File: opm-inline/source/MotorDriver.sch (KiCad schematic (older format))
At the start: 38 parts, among them IC1 TMC6200-TA, Q1 HYG025N06LS1C2, Q2 HYG025N06LS1C2, Q3 HYG025N06LS1C2, Q4 HYG025N06LS1C2, Q5 HYG025N06LS1C2, Q6 HYG025N06LS1C2

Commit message: update connections
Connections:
- net FAULT: now reaches IC1.26 (FAULT)
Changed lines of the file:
@@
 $Descr A4 11693 8268
 encoding utf-8
-Sheet 3 3
+Sheet 2 3
 Title "TMC6100-EVAL"
 Date "2019-10-28"
@@
 Text HLabel 3650 3400 0    28   Input ~ 0
 SPE
-Text HLabel 4750 3950 2    28   Input ~ 0
+Text HLabel 4750 3950 2    28   Output ~ 0
 ADC_I_u
-Text HLabel 4750 4000 2    28   Input ~ 0
+Text HLabel 4750 4000 2    28   Output ~ 0
 ADC_I_v
-Text HLabel 4750 4050 2    28   Input ~ 0
+Text HLabel 4750 4050 2    28   Output ~ 0
 ADC_I_w
 $Comp
@@
 	1    0    0    -1
 $EndComp
-Text HLabel 8750 2200 2    31   Input ~ 0
+Text HLabel 8750 2200 2    31   Output ~ 0
 U
 Wire Wire Line
 	8500 2200 8750 2200
-Text HLabel 10450 3500 2    31   Input ~ 0
+Text HLabel 10450 3500 2    31   Output ~ 0
 V
 Wire Wire Line
 	10150 3500 10450 3500
-Text HLabel 8800 5000 2    31   Input ~ 0
+Text HLabel 8800 5000 2    31   Output ~ 0
 W
 Wire Wire Line
@@
 	3650 3650 3450 3650
 $Comp
-L power:GND #PWR?
+L power:GND #PWR0109
 U 1 1 61F1E038
 P 3150 3550
-F 0 "#PWR?" H 3150 3300 39  0001 C CNN
+F 0 "#PWR0109" H 3150 3300 39  0001 C CNN
 F 1 "GND" H 3150 3400 39  0000 C CNN
 F 2 "" H 3150 3550 39  0001 C CNN
@@
 $EndComp
 $Comp
-L power:GND #PWR?
+L power:GND #PWR0113
 U 1 1 61F1F1E2
 P 3400 3500
-F 0 "#PWR?" H 3400 3250 39  0001 C CNN
+F 0 "#PWR0113" H 3400 3250 39  0001 C CNN
 F 1 "GND" H 3400 3350 39  0000 C CNN
 F 2 "" H 3400 3500 39  0001 C CNN
@@
 Wire Wire Line
 	3650 3500 3400 3500
+Text HLabel 4850 4400 3    28   Output ~ 0
+FAULT
+Text HLabel 4800 4400 3    28   Output ~ 0
+FAULT_LED
+Wire Wire Line
+	4800 4400 4800 4300
+Wire Wire Line
+	4800 4300 4750 4300
+Wire Wire Line
+	4800 4300 4850 4300
+Wire Wire Line
+	4850 4300 4850 4400
+Connection ~ 4800 4300
 $EndSCHEMATC

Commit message: rearrange
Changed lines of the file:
@@
 Text HLabel 4750 3950 2    28   Output ~ 0
 ADC_I_u
-Text HLabel 4750 4000 2    28   Output ~ 0
-ADC_I_v
 Text HLabel 4750 4050 2    28   Output ~ 0
 ADC_I_w
@@
 	4850 4300 4850 4400
 Connection ~ 4800 4300
+Text HLabel 4750 4000 2    31   Output ~ 0
+ADC_I_v
 $EndSCHEMATC

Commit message: use pins
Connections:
- net +VCC_IO: no longer IC1.16 (SDO_SINGLE)
- net GND: now also IC1.16 (SDO_SINGLE)
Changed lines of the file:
@@
 Wire Wire Line
 	8500 5000 8800 5000
-Text HLabel 3450 3650 0    31   Input ~ 0
-+VCC_IO
 Text HLabel 3450 3600 0    31   Input ~ 0
 +VCC_IO
@@
 Text HLabel 4850 4400 3    28   Output ~ 0
 FAULT
-Text HLabel 4800 4400 3    28   Output ~ 0
-FAULT_LED
-Wire Wire Line
-	4800 4400 4800 4300
-Wire Wire Line
-	4800 4300 4750 4300
-Wire Wire Line
-	4800 4300 4850 4300
 Wire Wire Line
 	4850 4300 4850 4400
-Connection ~ 4800 4300
 Text HLabel 4750 4000 2    31   Output ~ 0
 ADC_I_v
+$Comp
+L power:GND #PWR0106
+U 1 1 61E2421A
+P 3450 3650
+F 0 "#PWR0106" H 3450 3400 39  0001 C CNN
+F 1 "GND" H 3450 3500 39  0000 C CNN
+F 2 "" H 3450 3650 39  0001 C CNN
+F 3 "" H 3450 3650 39  0001 C CNN
+	1    3450 3650
+	1    0    0    -1
+$EndComp
+Wire Wire Line
+	4750 4300 4850 4300
 $EndSCHEMATC

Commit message: rearrange
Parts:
- added C21, C22, C23, C24, C25, C26: 1uF/100V, Capacitor_SMD:C_0805_2012Metric, symbol Device:C
- C7, C8, C9: value 4.7uF/100V -> 1uF/100V; footprint Capacitor_SMD:C_1210_3225Metric -> Capacitor_SMD:C_0805_2012Metric
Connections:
- net +VM: now also C21.1, C22.1, C23.1, C24.1, C25.1, C26.1
- net GND: now also C21.2, C22.2, C23.2, C24.2, C25.2, C26.2
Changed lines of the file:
@@
-	1    0    0    -1
-$EndComp
-$Comp
-L Device:C C8
-U 1 1 61C62AF0
-P 7700 4400
-F 0 "C8" H 7815 4435 35  0000 L CNN
-F 1 "4.7uF/100V" H 7815 4366 35  0000 L CNN
-F 2 "Capacitor_SMD:C_1210_3225Metric" H 7738 4250 50  0001 C CNN
-F 3 "https://datasheet.lcsc.com/lcsc/1912111437_Taiyo-Yuden-HMJ325AB7225KMHP_C412614.pdf" H 7700 4400 50  0001 C CNN
-F 4 "C697607" H 7700 4400 50  0001 C CNN "LCSC"
-F 5 "HMK325C7475KN-TE" H 7700 4400 50  0001 C CNN "manf_num  "
-	1    7700 4400
 	1    0    0    -1
 $EndComp
@@
 	0    1    1    0
 $EndComp
-$Comp
-L power:GND #PWR07
-U 1 1 61D8AF46
-P 8800 4200
-F 0 "#PWR07" H 8800 3950 50  0001 C CNN
-F 1 "GND" H 8805 4027 50  0000 C CNN
-F 2 "" H 8800 4200 50  0001 C CNN
-F 3 "" H 8800 4200 50  0001 C CNN
-	1    8800 4200
-	1    0    0    -1
-$EndComp
 Wire Wire Line
 	10150 3650 9900 3650
@@
 	10150 3500 10150 3650
 Connection ~ 10150 3500
-Wire Wire Line
-	8800 4100 8800 4200
 $Comp
 L power:GND #PWR08
@@
 F 3 "" H 9350 3000 50  0001 C CNN
 	1    9350 3000
-	1    0    0    -1
-$EndComp
-$Comp
-L Device:C C9
-U 1 1 61D8AF6F
-P 9350 2800
-F 0 "C9" H 9465 2835 35  0000 L CNN
-F 1 "4.7uF/100V" H 9465 2766 35  0000 L CNN
-F 2 "Capacitor_SMD:C_1210_3225Metric" H 9388 2650 50  0001 C CNN
-F 3 "https://datasheet.lcsc.com/lcsc/1912111437_Taiyo-Yuden-HMJ325AB7225KMHP_C412614.pdf" H 9350 2800 50  0001 C CNN
-F 4 "C697607" H 9350 2800 50  0001 C CNN "LCSC"
-F 5 "HMK325C7475KN-TE" H 9350 2800 50  0001 C CNN "manf_num  "
-	1    9350 2800
 	1    0    0    -1
 $EndComp
@@
 	8800 2550 9350 2550
 $Comp
-L Device:C C7
-U 1 1 61D9B6F4
-P 7700 1450
-F 0 "C7" H 7815 1485 35  0000 L CNN
-F 1 "4.7uF/100V" H 7815 1416 35  0000 L CNN
-F 2 "Capacitor_SMD:C_1210_3225Metric" H 7738 1300 50  0001 C CNN
-F 3 "https://datasheet.lcsc.com/lcsc/1912111437_Taiyo-Yuden-HMJ325AB7225KMHP_C412614.pdf" H 7700 1450 50  0001 C CNN
-F 4 "C697607" H 7700 1450 50  0001 C CNN "LCSC"
-F 5 "HMK325C7475KN-TE" H 7700 1450 50  0001 C CNN "manf_num  "
-	1    7700 1450
-	1    0    0    -1
-$EndComp
-$Comp
 L Device:R R1
 U 1 1 61D9B6BE
@@
 ADC_I_v
 $Comp
+L Device:C C9
+U 1 1 61D8AF6F
+P 9350 2800
+F 0 "C9" H 9465 2835 35  0000 L CNN
+F 1 "1uF/100V" H 9465 2766 35  0000 L CNN
+F 2 "Capacitor_SMD:C_0805_2012Metric" H 9388 2650 50  0001 C CNN
+F 3 "https://datasheet.lcsc.com/lcsc/1912111437_Taiyo-Yuden-HMJ325AB7225KMHP_C412614.pdf" H 9350 2800 50  0001 C CNN
+F 4 "C697607" H 9350 2800 50  0001 C CNN "LCSC"
+F 5 "HMK325C7475KN-TE" H 9350 2800 50  0001 C CNN "manf_num  "
+	1    9350 2800
+	1    0    0    -1
+$EndComp
+$Comp
+L Device:C C7
+U 1 1 61D9B6F4
+P 7700 1450
+F 0 "C7" H 7815 1485 35  0000 L CNN
+F 1 "1uF/100V" H 7815 1416 35  0000 L CNN
+F 2 "Capacitor_SMD:C_0805_2012Metric" H 7738 1300 50  0001 C CNN
+F 3 "https://datasheet.lcsc.com/lcsc/1912111437_Taiyo-Yuden-HMJ325AB7225KMHP_C412614.pdf" H 7700 1450 50  0001 C CNN
+F 4 "C697607" H 7700 1450 50  0001 C CNN "LCSC"
+F 5 "HMK325C7475KN-TE" H 7700 1450 50  0001 C CNN "manf_num  "
+	1    7700 1450
+	1    0    0    -1
+$EndComp
+$Comp
+L Device:C C8
+U 1 1 61C62AF0
+P 7700 4400
+F 0 "C8" H 7815 4435 35  0000 L CNN
+F 1 "1uF/100V" H 7815 4366 35  0000 L CNN
+F 2 "Capacitor_SMD:C_0805_2012Metric" H 7738 4250 50  0001 C CNN
+F 3 "https://datasheet.lcsc.com/lcsc/1912111437_Taiyo-Yuden-HMJ325AB7225KMHP_C412614.pdf" H 7700 4400 50  0001 C CNN
+F 4 "C697607" H 7700 4400 50  0001 C CNN "LCSC"
+F 5 "HMK325C7475KN-TE" H 7700 4400 50  0001 C CNN "manf_num  "
+	1    7700 4400
+	1    0    0    -1
+$EndComp
+Wire Wire Line
+	4800 4300 4850 4300
+Wire Wire Line
+	4800 4300 4750 4300
+Connection ~ 4800 4300
+Wire Wire Line
+	4800 4400 4800 4300
+Text HLabel 4800 4400 3    28   Output ~ 0
+FAULT_LED
+$Comp
 L power:GND #PWR0106
 U 1 1 61E2421A
@@
 	1    0    0    -1
 $EndComp
-Wire Wire Line
-	4750 4300 4850 4300
+$Comp
+L Device:C C21
+U 1 1 61D83737
+P 8250 1450
+F 0 "C21" H 8365 1485 35  0000 L CNN
+F 1 "1uF/100V" H 8365 1416 35  0000 L CNN
+F 2 "Capacitor_SMD:C_0805_2012Metric" H 8288 1300 50  0001 C CNN
+F 3 "https://datasheet.lcsc.com/lcsc/1912111437_Taiyo-Yuden-HMJ325AB7225KMHP_C412614.pdf" H 8250 1450 50  0001 C CNN
+F 4 "C697607" H 8250 1450 50  0001 C CNN "LCSC"
+F 5 "HMK325C7475KN-TE" H 8250 1450 50  0001 C CNN "manf_num  "
+	1    8250 1450
+	1    0    0    -1
+$EndComp
+$Comp
+L Device:C C23
+U 1 1 61D8411C
+P 8800 1450
+F 0 "C23" H 8915 1485 35  0000 L CNN
+F 1 "1uF/100V" H 8915 1416 35  0000 L CNN
+F 2 "Capacitor_SMD:C_0805_2012Metric" H 8838 1300 50  0001 C CNN
+F 3 "https://datasheet.lcsc.com/lcsc/1912111437_Taiyo-Yuden-HMJ325AB7225KMHP_C412614.pdf" H 8800 1450 50  0001 C CNN
+F 4 "C697607" H 8800 1450 50  0001 C CNN "LCSC"
+F 5 "HMK325C7475KN-TE" H 8800 1450 50  0001 C CNN "manf_num  "
+	1    8800 1450
+	1    0    0    -1
+$EndComp
+Wire Wire Line
+	7700 1200 8250 1200
+Wire Wire Line
+	8250 1200 8250 1300
+Connection ~ 7700 1200
+Wire Wire Line
+	8800 1300 8800 1200
+Wire Wire Line
+	8800 1200 8250 1200
+Connection ~ 8250 1200
+Wire Wire Line
+	7700 1650 8250 1650
+Wire Wire Line
+	8250 1650 8250 1600
+Connection ~ 7700 1650
+Wire Wire Line
+	8250 1650 8800 1650
+Wire Wire Line
+	8800 1650 8800 1600
+Connection ~ 8250 1650
+$Comp
+L Device:C C25
+U 1 1 61DA3602
+P 9900 2800
+F 0 "C25" H 10015 2835 35  0000 L CNN
+F 1 "1uF/100V" H 10015 2766 35  0000 L CNN
+F 2 "Capacitor_SMD:C_0805_2012Metric" H 9938 2650 50  0001 C CNN
+F 3 "https://datasheet.lcsc.com/lcsc/1912111437_Taiyo-Yuden-HMJ325AB7225KMHP_C412614.pdf" H 9900 2800 50  0001 C CNN
+F 4 "C697607" H 9900 2800 50  0001 C CNN "LCSC"
+F 5 "HMK325C7475KN-TE" H 9900 2800 50  0001 C CNN "manf_num  "
+	1    9900 2800
+	1    0    0    -1
+$EndComp
+$Comp
+L Device:C C26
+U 1 1 61DA3EE3
+P 10500 2800
+F 0 "C26" H 10615 2835 35  0000 L CNN
+F 1 "1uF/100V" H 10615 2766 35  0000 L CNN
+F 2 "Capacitor_SMD:C_0805_2012Metric" H 10538 2650 50  0001 C CNN
+F 3 "https://datasheet.lcsc.com/lcsc/1912111437_Taiyo-Yuden-HMJ325AB7225KMHP_C412614.pdf" H 10500 2800 50  0001 C CNN
+F 4 "C697607" H 10500 2800 50  0001 C CNN "LCSC"
+F 5 "HMK325C7475KN-TE" H 10500 2800 50  0001 C CNN "manf_num  "
+	1    10500 2800
+	1    0    0    -1
+$EndComp
+Wire Wire Line
+	9350 2550 9900 2550
+Wire Wire Line
+	9900 2550 9900 2650
+Connection ~ 9350 2550
+Wire Wire Line
+	9900 2550 10500 2550
+Wire Wire Line
+	10500 2550 10500 2650
+Connection ~ 9900 2550
+Wire Wire Line
+	9350 3000 9900 3000
+Wire Wire Line
+	9900 3000 9900 2950
+Connection ~ 9350 3000
+Wire Wire Line
+	9900 3000 10500 3000
+Wire Wire Line
+	10500 3000 10500 2950
+Connection ~ 9900 3000
+$Comp
+L Device:C C22
+U 1 1 61DC56F3
+P 8250 4400
+F 0 "C22" H 8365 4435 35  0000 L CNN
+F 1 "1uF/100V" H 8365 4366 35  0000 L CNN
+F 2 "Capacitor_SMD:C_0805_2012Metric" H 8288 4250 50  0001 C CNN
+F 3 "https://datasheet.lcsc.com/lcsc/1912111437_Taiyo-Yuden-HMJ325AB7225KMHP_C412614.pdf" H 8250 4400 50  0001 C CNN
+F 4 "C697607" H 8250 4400 50  0001 C CNN "LCSC"
+F 5 "HMK325C7475KN-TE" H 8250 4400 50  0001 C CNN "manf_num  "
+	1    8250 4400
+	1    0    0    -1
+$EndComp
+$Comp
+L Device:C C24
+U 1 1 61DC6076
+P 9000 4400
+F 0 "C24" H 9115 4435 35  0000 L CNN
+F 1 "1uF/100V" H 9115 4366 35  0000 L CNN
+F 2 "Capacitor_SMD:C_0805_2012Metric" H 9038 4250 50  0001 C CNN
+F 3 "https://datasheet.lcsc.com/lcsc/1912111437_Taiyo-Yuden-HMJ325AB7225KMHP_C412614.pdf" H 9000 4400 50  0001 C CNN
+F 4 "C697607" H 9000 4400 50  0001 C CNN "LCSC"
+F 5 "HMK325C7475KN-TE" H 9000 4400 50  0001 C CNN "manf_num  "
+	1    9000 4400
+	1    0    0    -1
+$EndComp
+$Comp
+L power:GND #PWR07
+U 1 1 61DC79BF
+P 8800 4100
+F 0 "#PWR07" H 8800 3850 50  0001 C CNN
+F 1 "GND" H 8805 3927 50  0000 C CNN
+F 2 "" H 8800 4100 50  0001 C CNN
+F 3 "" H 8800 4100 50  0001 C CNN
+	1    8800 4100
+	1    0    0    -1
+$EndComp
+Wire Wire Line
+	8250 4250 8250 4150
+Wire Wire Line
+	8250 4150 7700 4150
+Connection ~ 7700 4150
+Wire Wire Line
+	8250 4150 9000 4150
+Wire Wire Line
+	9000 4150 9000 4250
+Connection ~ 8250 4150
+Wire Wire Line
+	7700 4600 8250 4600
+Wire Wire Line
+	8250 4600 8250 4550
+Connection ~ 7700 4600
+Wire Wire Line
+	8250 4600 9000 4600
+Wire Wire Line
+	9000 4600 9000 4550
+Connection ~ 8250 4600
 $EndSCHEMATC

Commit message: esd
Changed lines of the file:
@@
 	1    0    0    -1
 $EndComp
-Wire Wire Line
-	4800 4300 4850 4300
-Wire Wire Line
-	4800 4300 4750 4300
-Connection ~ 4800 4300
-Wire Wire Line
-	4800 4400 4800 4300
-Text HLabel 4800 4400 3    28   Output ~ 0
-FAULT_LED
 $Comp
 L power:GND #PWR0106
@@
 	9000 4600 9000 4550
 Connection ~ 8250 4600
+Wire Wire Line
+	4750 4300 4850 4300
 $EndSCHEMATC

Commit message: update
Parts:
- IC1: Field5 TMC6200-TA -> (none); manf_num (none) -> TMC6200-TA
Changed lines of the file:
@@
 F 3 "https://trinamic.com/fileadmin/assets/Products/ICs_Documents/TMC6200_datasheet_Rev1.05.pdf" H 4200 4475 40  0001 C CNN
 F 4 "" H 4200 3650 50  0001 C CNN "LCSC"
-F 5 "TMC6200-TA" H 4200 3650 50  0001 C CNN "Field5"
+F 5 "TMC6200-TA" H 4200 3650 50  0001 C CNN "manf_num"
 F 6 "No" H 4200 3650 50  0001 C CNN "JLCPCB BOM"
 	1    4200 3650

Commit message: fix current sense resistor
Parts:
- R10, R14, R15, R7, R8, R9: LCSC C2692048 -> C601096; manf_num SME12ABFR005T -> HoLR1206-1W-5mR-1%-75ppm
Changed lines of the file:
@@
 F 1 "0R005/1%/1W" V 7995 4850 35  0000 C CNN
 F 2 "Resistor_SMD:R_1206_3216Metric" V 8030 4850 50  0001 C CNN
-F 3 "https://datasheet.lcsc.com/lcsc/2106062334_SART-Nanjing-Sart-Tech-SME12ABFR005T_C2692048.pdf" H 8100 4850 50  0001 C CNN
-F 4 "C2692048" V 8100 4850 50  0001 C CNN "LCSC"
-F 5 "SME12ABFR005T" V 8100 4850 50  0001 C CNN "manf_num"
+F 3 "https://datasheet.lcsc.com/lcsc/2006112327_Milliohm-HoLR1206-1W-5mR-1--75ppm_C601096.pdf" H 8100 4850 50  0001 C CNN
+F 4 "C601096" V 8100 4850 50  0001 C CNN "LCSC"
+F 5 "HoLR1206-1W-5mR-1%-75ppm" V 8100 4850 50  0001 C CNN "manf_num"
 	1    8100 4850
 	0    1    1    0
@@
 F 1 "0R005/1%/1W" V 7995 5150 35  0000 C CNN
 F 2 "Resistor_SMD:R_1206_3216Metric" V 8030 5150 50  0001 C CNN
-F 3 "https://datasheet.lcsc.com/lcsc/2106062334_SART-Nanjing-Sart-Tech-SME12ABFR005T_C2692048.pdf" H 8100 5150 50  0001 C CNN
-F 4 "C2692048" V 8100 5150 50  0001 C CNN "LCSC"
-F 5 "SME12ABFR005T" V 8100 5150 50  0001 C CNN "manf_num"
+F 3 "https://datasheet.lcsc.com/lcsc/2006112327_Milliohm-HoLR1206-1W-5mR-1--75ppm_C601096.pdf" H 8100 5150 50  0001 C CNN
+F 4 "C601096" V 8100 5150 50  0001 C CNN "LCSC"
+F 5 "HoLR1206-1W-5mR-1%-75ppm" V 8100 5150 50  0001 C CNN "manf_num"
 	1    8100 5150
 	0    1    1    0
@@
 F 1 "0R005/1%/1W" V 9645 3350 35  0000 C CNN
 F 2 "Resistor_SMD:R_1206_3216Metric" V 9680 3350 50  0001 C CNN
-F 3 "https://datasheet.lcsc.com/lcsc/2106062334_SART-Nanjing-Sart-Tech-SME12ABFR005T_C2692048.pdf" H 9750 3350 50  0001 C CNN
-F 4 "C2692048" V 9750 3350 50  0001 C CNN "LCSC"
-F 5 "SME12ABFR005T" V 9750 3350 50  0001 C CNN "manf_num"
+F 3 "https://datasheet.lcsc.com/lcsc/2006112327_Milliohm-HoLR1206-1W-5mR-1--75ppm_C601096.pdf" H 9750 3350 50  0001 C CNN
+F 4 "C601096" V 9750 3350 50  0001 C CNN "LCSC"
+F 5 "HoLR1206-1W-5mR-1%-75ppm" V 9750 3350 50  0001 C CNN "manf_num"
 	1    9750 3350
 	0    1    1    0
@@
 F 1 "0R005/1%/1W" V 9645 3650 35  0000 C CNN
 F 2 "Resistor_SMD:R_1206_3216Metric" V 9680 3650 50  0001 C CNN
-F 3 "https://datasheet.lcsc.com/lcsc/2106062334_SART-Nanjing-Sart-Tech-SME12ABFR005T_C2692048.pdf" H 9750 3650 50  0001 C CNN
-F 4 "C2692048" V 9750 3650 50  0001 C CNN "LCSC"
-F 5 "SME12ABFR005T" V 9750 3650 50  0001 C CNN "manf_num"
+F 3 "https://datasheet.lcsc.com/lcsc/2006112327_Milliohm-HoLR1206-1W-5mR-1--75ppm_C601096.pdf" H 9750 3650 50  0001 C CNN
+F 4 "C601096" V 9750 3650 50  0001 C CNN "LCSC"
+F 5 "HoLR1206-1W-5mR-1%-75ppm" V 9750 3650 50  0001 C CNN "manf_num"
 	1    9750 3650
 	0    1    1    0
@@
 F 1 "0R005/1%/1W" V 7995 2050 35  0000 C CNN
 F 2 "Resistor_SMD:R_1206_3216Metric" V 8030 2050 50  0001 C CNN
-F 3 "https://datasheet.lcsc.com/lcsc/2106062334_SART-Nanjing-Sart-Tech-SME12ABFR005T_C2692048.pdf" H 8100 2050 50  0001 C CNN
-F 4 "C2692048" V 8100 2050 50  0001 C CNN "LCSC"
-F 5 "SME12ABFR005T" V 8100 2050 50  0001 C CNN "manf_num"
+F 3 "https://datasheet.lcsc.com/lcsc/2006112327_Milliohm-HoLR1206-1W-5mR-1--75ppm_C601096.pdf" H 8100 2050 50  0001 C CNN
+F 4 "C601096" V 8100 2050 50  0001 C CNN "LCSC"
+F 5 "HoLR1206-1W-5mR-1%-75ppm" V 8100 2050 50  0001 C CNN "manf_num"
 	1    8100 2050
 	0    1    1    0
@@
 F 1 "0R005/1%/1W" V 7995 2350 35  0000 C CNN
 F 2 "Resistor_SMD:R_1206_3216Metric" V 8030 2350 50  0001 C CNN
-F 3 "https://datasheet.lcsc.com/lcsc/2106062334_SART-Nanjing-Sart-Tech-SME12ABFR005T_C2692048.pdf" H 8100 2350 50  0001 C CNN
-F 4 "C2692048" V 8100 2350 50  0001 C CNN "LCSC"
-F 5 "SME12ABFR005T" V 8100 2350 50  0001 C CNN "manf_num"
+F 3 "https://datasheet.lcsc.com/lcsc/2006112327_Milliohm-HoLR1206-1W-5mR-1--75ppm_C601096.pdf" H 8100 2350 50  0001 C CNN
+F 4 "C601096" V 8100 2350 50  0001 C CNN "LCSC"
+F 5 "HoLR1206-1W-5mR-1%-75ppm" V 8100 2350 50  0001 C CNN "manf_num"
 	1    8100 2350
 	0    1    1    0

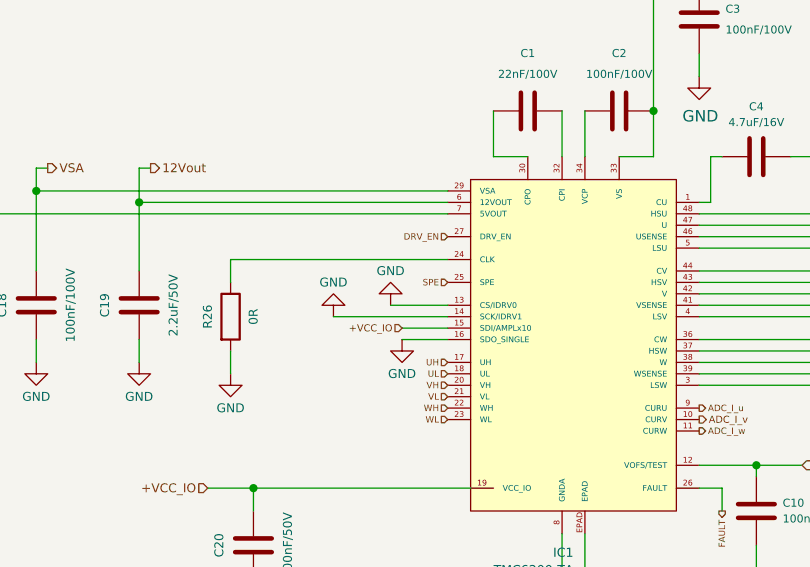
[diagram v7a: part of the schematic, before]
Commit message: tie spe low for standalone
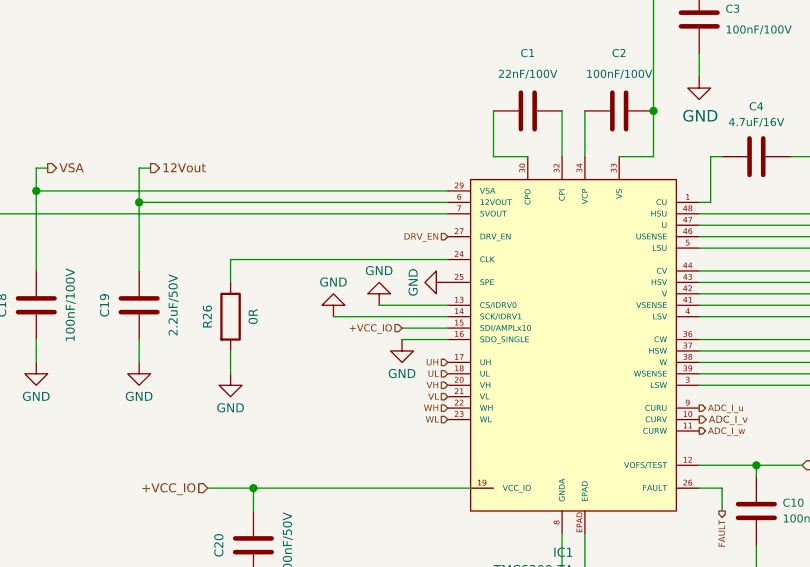
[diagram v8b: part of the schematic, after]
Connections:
- net SPE is gone; now on net GND: IC1.25 (SPE)
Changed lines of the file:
@@
 Text HLabel 3650 3200 0    28   Input ~ 0
 DRV_EN
-Text HLabel 3650 3400 0    28   Input ~ 0
-SPE
 Text HLabel 4750 3950 2    28   Output ~ 0
 ADC_I_u
@@
 L power:GND #PWR0113
 U 1 1 61F1F1E2
-P 3400 3500
-F 0 "#PWR0113" H 3400 3250 39  0001 C CNN
-F 1 "GND" H 3400 3350 39  0000 C CNN
-F 2 "" H 3400 3500 39  0001 C CNN
-F 3 "" H 3400 3500 39  0001 C CNN
-	1    3400 3500
+P 3350 3500
+F 0 "#PWR0113" H 3350 3250 39  0001 C CNN
+F 1 "GND" H 3350 3350 39  0000 C CNN
+F 2 "" H 3350 3500 39  0001 C CNN
+F 3 "" H 3350 3500 39  0001 C CNN
+	1    3350 3500
 	-1   0    0    1
 $EndComp
 Wire Wire Line
 	3650 3550 3150 3550
-Wire Wire Line
-	3650 3500 3400 3500
 Text HLabel 4850 4400 3    28   Output ~ 0
 FAULT
@@
 Wire Wire Line
 	4750 4300 4850 4300
+$Comp
+L power:GND #PWR?
+U 1 1 61E9D2B7
+P 3650 3400
+F 0 "#PWR?" H 3650 3150 39  0001 C CNN
+F 1 "GND" H 3650 3250 39  0000 C CNN
+F 2 "" H 3650 3400 39  0001 C CNN
+F 3 "" H 3650 3400 39  0001 C CNN
+	1    3650 3400
+	0    1    1    0
+$EndComp
+Wire Wire Line
+	3350 3500 3650 3500
 $EndSCHEMATC
